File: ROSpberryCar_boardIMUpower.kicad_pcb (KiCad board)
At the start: 2 copper layers, 32.3 x 33.3 mm, 5 parts, among them P1 CONN_5, P2 CONN_5, P3 RASPI_CONN, P4 CONN_2, P5 CONN_5

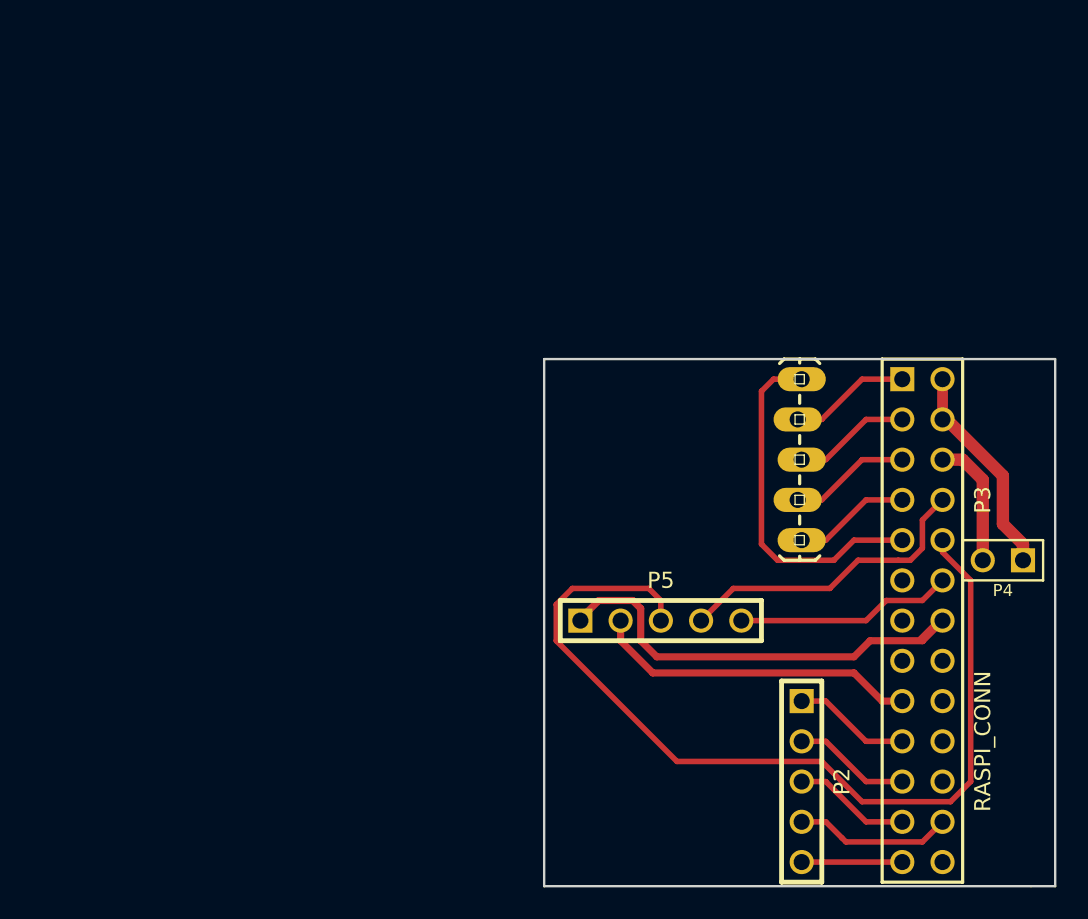
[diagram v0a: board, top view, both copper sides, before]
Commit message: svg exported, added led
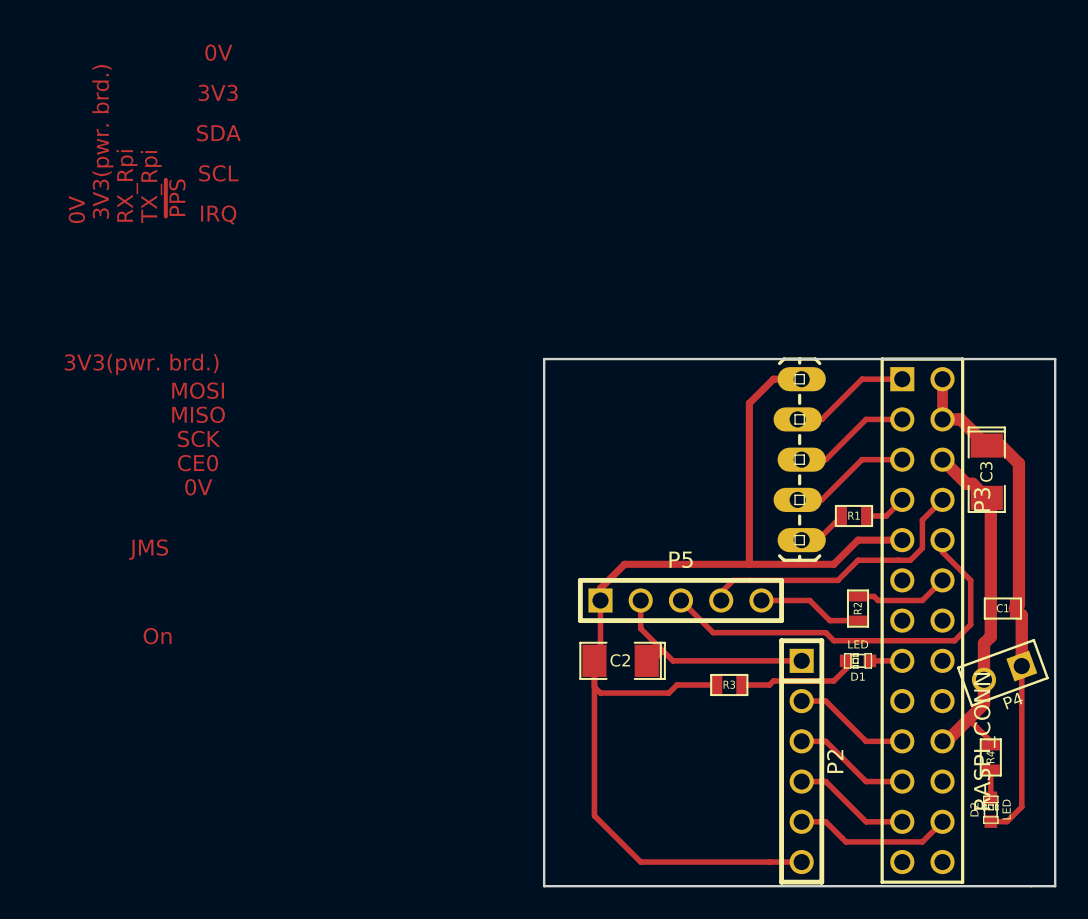
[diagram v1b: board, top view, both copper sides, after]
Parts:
- added C1: C, SM0603, F.Cu at (195.6, 103.4)
- added C2: C, SM1206POL, F.Cu at (171.4, 106.7)
- added C3: C, SM1206POL, F.Cu at (194.6, 94.7)
- added D1: LED, LED-0603, F.Cu at (186.4, 106.7)
- added D2: LED, LED-0603, F.Cu at (194.8, 116.1)
- added R1: R, SM0603, F.Cu at (186.2, 97.5)
- added R2: R, SM0603, F.Cu at (186.4, 103.4)
- added R3: R, SM0603, F.Cu at (178.3, 108.2)
- added R4: R, SM0603, F.Cu at (194.8, 112.8)
- P2: value CONN_5 -> CONN_6; footprint PIN_ARRAY_5x1 -> PIN_ARRAY-6X1
- moved P4 7.11 mm to (195.6, 107.4), turned to 200 degrees
- moved P5 1.80 mm to (175.3, 102.9)
- moved P2 1.27 mm to (182.9, 113.0)
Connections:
- P1 pad 1: N-000004 -> N-0000022
- P1 pad 5: N-000005 -> N-000002
- P2 pad 1: N-0000017 (its old number) -> N-000008
- P2 pad 2: N-0000016 -> N-000009
- P2 pad 3: N-0000015 -> N-0000019
- P2 pad 4: N-0000014 -> N-0000016
- P2 pad 5: N-0000011 -> N-000001
- P3 pad 12: N-000001 -> N-000004
- P3 pad 14: N-0000013 (its old number) -> N-0000015
- P3 pad 17: N-0000012 (its old number) -> N-0000011
- P3 pad 19: N-0000017 (its old number) -> N-000009
- P3 pad 20: N-0000021 -> /gnd
- P3 pad 21: N-0000016 -> N-0000019
- P3 pad 23: N-0000015 -> N-0000016
- P3 pad 24: N-0000014 -> N-000001
- P3 pad 25: N-0000011 -> N-0000014
- P3 pad 6: N-0000010 (its old number) -> /gnd
- P3 pad 7: N-000005 -> N-000003
- P3 pad 9: N-000004 -> N-0000022
- P4 pad 2: N-0000010 (its old number) -> /gnd
- P5 pad 1: N-0000013 (its old number) -> N-0000022
- P5 pad 2: N-0000012 (its old number) -> N-000008
- P5 pad 5: N-000001 -> N-0000028
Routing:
- net N-0000022: track 0.00 -> 73.0 mm
- net N-0000013 (its old number): track 50.2 -> 0.00 mm
- net N-0000029: track 57.8 -> 25.8 mm
- net /gnd: track 0.00 -> 22.9 mm
- net N-0000012 (its old number): track 20.6 -> 0.00 mm
- net N-0000026: track 13.7 -> 32.8 mm
- net N-000004: track 22.3 -> 5.97 mm
- net N-000008: track 0.00 -> 14.1 mm
- net N-0000014: track 9.94 -> 0.00 mm
- net N-0000010 (its old number): track 8.15 -> 0.00 mm
- net N-000009: track 0.00 -> 7.40 mm
- net N-0000017 (its old number): track 7.40 -> 0.00 mm
- net N-0000015: track 7.40 -> 0.00 mm
- net N-0000019: track 0.00 -> 7.40 mm
- net N-0000028: track 0.00 -> 6.62 mm
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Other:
- board text added: "0V"
- board text added: "3V3"
- board text added: "3V3(pwr. brd.)"
- board text added: "CE0"
- board text added: "IRQ"
- board text added: "JMS"
- board text added: "MISO"
- board text added: "MOSI"
- board text added: "On"
- board text added: "RX_Rpi"
- board text added: "SCK"
- board text added: "SCL"
- board text added: "SDA"
- board text added: "TX_Rpi"
- board text added: "~PPS"

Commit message: larger pads
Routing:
- net N-0000023: track 17.9 -> 19.3 mm
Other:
- net class Default: clearance 0.254 -> 0.23
- rule trace_clearance: 0.254 -> 0.23

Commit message: v2
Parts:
- removed R2, R3: R, SM0603
- P1: value CONN_5 -> CONN_4; footprint SparkFun-1X05_LOCK_LONGPADS -> SparkFun-1X04-SMD
- P2: footprint PIN_ARRAY-6X1 -> SparkFun-1X06_LOCK
- P5: value CONN_5 -> CONN_4; footprint PIN_ARRAY_5x1 -> SparkFun-1X04_LOCK
- moved P1 20.3 mm to (178.6, 108.7), turned to 90 degrees
- moved P2 15.5 mm to (168.7, 119.1), turned to 0 degrees
- moved C2 7.75 mm to (175.5, 100.1)
- moved P5 5.14 mm to (170.9, 100.1), turned to 90 degrees
- moved R1 4.75 mm to (184.9, 102.1), turned to 180 degrees
- moved D1 2.96 mm to (184.9, 104.1)
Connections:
- C2 pad 2: N-0000022 (its old number) -> /gnd
- D1 pad 1: N-000006 (its old number) -> N-000003
- D1 pad 2: N-000005 (its old number) -> N-000002
- P1 pad 1: N-0000022 (its old number) -> /gnd
- P1 pad 2: N-0000027 -> /3v3_2
- P2 pad 6: N-0000022 (its old number) -> N-000004
- P3 pad 1: N-0000027 -> N-0000024
- P3 pad 13: N-0000017 (its old number) -> N-000003
- P3 pad 15: N-000006 (its old number) -> N-0000014
- P3 pad 17: N-0000011 (its old number) -> /3v3_2
- P3 pad 25: N-0000014 -> N-000004
- P3 pad 7: N-000003 -> N-0000021
- P3 pad 9: N-0000022 (its old number) -> /gnd
- P5 pad 1: N-0000022 (its old number) -> /gnd
- R1 pad 1: N-000002 -> /gnd
- R1 pad 2: N-000003 -> N-000002
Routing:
- net N-0000022 (its old number): track 73.0 -> 0.00 mm
- net /gnd: track 22.9 -> 80.3 mm
- net N-0000023: track 7.40 -> 42.5 mm
- net N-0000022: track 7.66 -> 39.2 mm
- net N-000006: track 14.1 -> 33.5 mm
- net /3v3_2: track 0.00 -> 16.0 mm
- net N-0000010: track 7.40 -> 21.2 mm
- net N-000009: track 7.40 -> 17.5 mm
- net N-000004: track 0.00 -> 7.87 mm
- net N-0000027: track 7.66 -> 0.00 mm
- net N-000005 (its old number): track 7.54 -> 0.00 mm
- net N-0000028: track 6.62 -> 0.00 mm
- net N-0000016: track 7.40 -> 14.0 mm
- net N-0000018: track 5.97 -> 0.00 mm
- net N-000001: track 9.94 -> 14.6 mm
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- added copper zone on F.Cu, net /gnd
- removed copper zone on F.Cu, net (none)
